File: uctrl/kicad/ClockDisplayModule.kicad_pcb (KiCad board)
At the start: 2 copper layers, 94 x 58.4 mm, 49 parts, among them IC1 ATMEGA88PA-A, P101 CONN_02X03, P102 CONN_01X06, P201 CONN_01X06, P202 CONN_01X07, P203 CONN_01X06, P204 CONN_01X07, Q201 BC856BS, Q202 BC856BS, Q203 BC856BS, SW101 TL3315NF160Q, U201 SN74LS138, U202 74HC4511

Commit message: Updated the revision number
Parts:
- moved P203 2.54 mm to (119.4, 81.3)
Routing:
- net C_Signal: track 7.02 -> 7.72 mm
- net C_Dig_1: track 7.20 -> 7.79 mm
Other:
- board text added: "Clock display Module 2L.5 Control board"
- board text added: "Clock display Module 2L.5 Display board"
- board text removed: "Clock display Module 2L.4 Control board"
- board text removed: "Clock display Module 2L.4 Display board"
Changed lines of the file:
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@@
-(kicad_pcb (version 4) (host pcbnew 4.0.0-stable)
+(kicad_pcb (version 4) (host pcbnew 4.0.0-2.201512072331+6194~38~ubuntu14.04.1-stable)
   (general
     (links 171)
@@
     (thickness 1.6)
     (drawings 25)
-    (tracks 571)
+    (tracks 566)
     (zones 0)
     (modules 49)
@@
   (title_block
     (title "Clock Display Module")
-    (rev 4L.2)
+    (date 2016-05-05)
+    (rev 2L.5)
   )
   (layers
@@
   )
   (setup
-    (last_trace_width 0.1524)
+    (last_trace_width 0.3048)
     (user_trace_width 0.3048)
     (user_trace_width 0.6096)
@@
   )
   (module Pin_Headers:Pin_Header_Straight_1x06 (layer B.Cu)
-    (at 119.38 83.82 180)
+    (at 119.38 81.28 180)
     (descr "Through hole pin header")
     (tags "pin header")
@@
   (gr_line (start 207.01 100.33) (end 115.57 100.33) (angle 90) (layer Edge.Cuts) (width 2.54))
   (gr_line (start 115.57 41.91) (end 207.01 41.91) (angle 90) (layer Edge.Cuts) (width 2.54))
-  (gr_text "Clock display Module 2L.4\nControl board" (at 118.237 80.518) (layer F.SilkS)
+  (gr_text "Clock display Module 2L.5\nControl board" (at 121.666 80.518) (layer F.SilkS)
     (effects (font (size 0.762 0.762) (thickness 0.127)) (justify left))
   )
-  (gr_text "Clock display Module 2L.4\nDisplay board" (at 135.89 73.152) (layer B.SilkS)
+  (gr_text "Clock display Module 2L.5\nDisplay board" (at 135.89 73.152) (layer B.SilkS)
     (effects (font (size 0.762 0.762) (thickness 0.127)) (justify left mirror))
   )
@@
   (segment (start 169.672 93.599) (end 169.672 93.726) (width 0.3048) (layer F.Cu) (net 22))
   (segment (start 155.255 91.178) (end 155.442 90.991) (width 0.3048) (layer F.Cu) (net 22) (status 30))
-  (segment (start 119.38 83.82) (end 121.412 83.82) (width 0.3048) (layer F.Cu) (net 23))
-  (segment (start 121.412 83.82) (end 122.809 82.423) (width 0.3048) (layer F.Cu) (net 23))
-  (segment (start 122.809 82.423) (end 127 82.423) (width 0.3048) (layer F.Cu) (net 23))
-  (segment (start 127 82.423) (end 127.65 83.073) (width 0.3048) (layer F.Cu) (net 23))
-  (segment (start 127.65 83.073) (end 127.65 84.1255) (width 0.3048) (layer F.Cu) (net 23))
-  (segment (start 119.38 86.36) (end 121.539 86.36) (width 0.3048) (layer F.Cu) (net 24))
-  (segment (start 121.539 86.36) (end 122.0985 85.8005) (width 0.3048) (layer F.Cu) (net 24))
-  (segment (start 122.0985 85.8005) (end 126.35 85.8005) (width 0.3048) (layer F.Cu) (net 24))
-  (segment (start 119.38 88.9) (end 123.571 88.9) (width 0.3048) (layer F.Cu) (net 25))
-  (segment (start 123.571 88.9) (end 124.587 87.884) (width 0.3048) (layer F.Cu) (net 25))
-  (segment (start 124.587 87.884) (end 127.254 87.884) (width 0.3048) (layer F.Cu) (net 25))
-  (segment (start 127.254 87.884) (end 127.65 88.28) (width 0.3048) (layer F.Cu) (net 25))
-  (segment (start 127.65 88.28) (end 127.65 89.0785) (width 0.3048) (layer F.Cu) (net 25))
-  (segment (start 119.38 91.44) (end 124.079 91.44) (width 0.3048) (layer F.Cu) (net 26))
-  (segment (start 124.079 91.44) (end 124.7655 90.7535) (width 0.3048) (layer F.Cu) (net 26))
-  (segment (start 124.7655 90.7535) (end 126.35 90.7535) (width 0.3048) (layer F.Cu) (net 26))
-  (segment (start 119.38 93.98) (end 123.063 93.98) (width 0.3048) (layer F.Cu) (net 27))
-  (segment (start 123.063 93.98) (end 123.825 93.218) (width 0.3048) (layer F.Cu) (net 27))
-  (segment (start 123.825 93.218) (end 127.127 93.218) (width 0.3048) (layer F.Cu) (net 27))
-  (segment (start 127.127 93.218) (end 127.523 93.614) (width 0.3048) (layer F.Cu) (net 27))
-  (segment (start 127.523 93.614) (end 127.523 94.4125) (width 0.3048) (layer F.Cu) (net 27))
-  (segment (start 119.38 96.52) (end 123.952 96.52) (width 0.3048) (layer F.Cu) (net 28))
-  (segment (start 123.952 96.52) (end 124.3845 96.0875) (width 0.3048) (layer F.Cu) (net 28))
-  (segment (start 124.3845 96.0875) (end 126.223 96.0875) (width 0.3048) (layer F.Cu) (net 28))
+  (segment (start 127.65 84.1255) (end 127.65 83.073) (width 0.3048) (layer F.Cu) (net 23) (status 400000))
+  (segment (start 125.857 81.28) (end 119.38 81.28) (width 0.3048) (layer F.Cu) (net 23) (status 800000))
+  (segment (start 127.65 83.073) (end 125.857 81.28) (width 0.3048) (layer F.Cu) (net 23))
+  (segment (start 126.35 85.8005) (end 124.7895 85.8005) (width 0.3048) (layer F.Cu) (net 24) (status 400000))
+  (segment (start 122.809 83.82) (end 119.38 83.82) (width 0.3048) (layer F.Cu) (net 24) (status 800000))
+  (segment (start 124.7895 85.8005) (end 122.809 83.82) (width 0.3048) (layer F.Cu) (net 24))
+  (segment (start 127.65 89.0785) (end 127.65 88.407) (width 0.3048) (layer F.Cu) (net 25) (status 400000))
+  (segment (start 125.603 86.36) (end 119.38 86.36) (width 0.3048) (layer F.Cu) (net 25) (status 800000))
+  (segment (start 127.65 88.407) (end 125.603 86.36) (width 0.3048) (layer F.Cu) (net 25))
+  (segment (start 126.35 90.7535) (end 124.7895 90.7535) (width 0.3048) (layer F.Cu) (net 26) (status 400000))
+  (segment (start 122.936 88.9) (end 119.38 88.9) (width 0.3048) (layer F.Cu) (net 26) (status 800000))
+  (segment (start 124.7895 90.7535) (end 122.936 88.9) (width 0.3048) (layer F.Cu) (net 26))
+  (segment (start 127.523 94.4125) (end 127.508 94.3975) (width 0.3048) (layer F.Cu) (net 27) (status C00000))
+  (segment (start 127.508 94.3975) (end 127.508 93.726) (width 0.3048) (layer F.Cu) (net 27) (status 400000))
+  (segment (start 127.508 93.726) (end 125.349 91.567) (width 0.3048) (layer F.Cu) (net 27))
+  (segment (start 125.349 91.567) (end 119.507 91.567) (width 0.3048) (layer F.Cu) (net 27) (status 800000))
+  (segment (start 119.507 91.567) (end 119.38 91.44) (width 0.3048) (layer F.Cu) (net 27) (status C00000))
+  (segment (start 126.223 96.0875) (end 124.1155 93.98) (width 0.3048) (layer F.Cu) (net 28) (status 400000))
+  (segment (start 124.1155 93.98) (end 119.38 93.98) (width 0.3048) (layer F.Cu) (net 28) (status 800000))
   (segment (start 132 83.82) (end 129.667 83.82) (width 0.3048) (layer F.Cu) (net 29))
   (segment (start 129.667 83.82) (end 128.524 84.963) (width 0.3048) (layer F.Cu) (net 29))

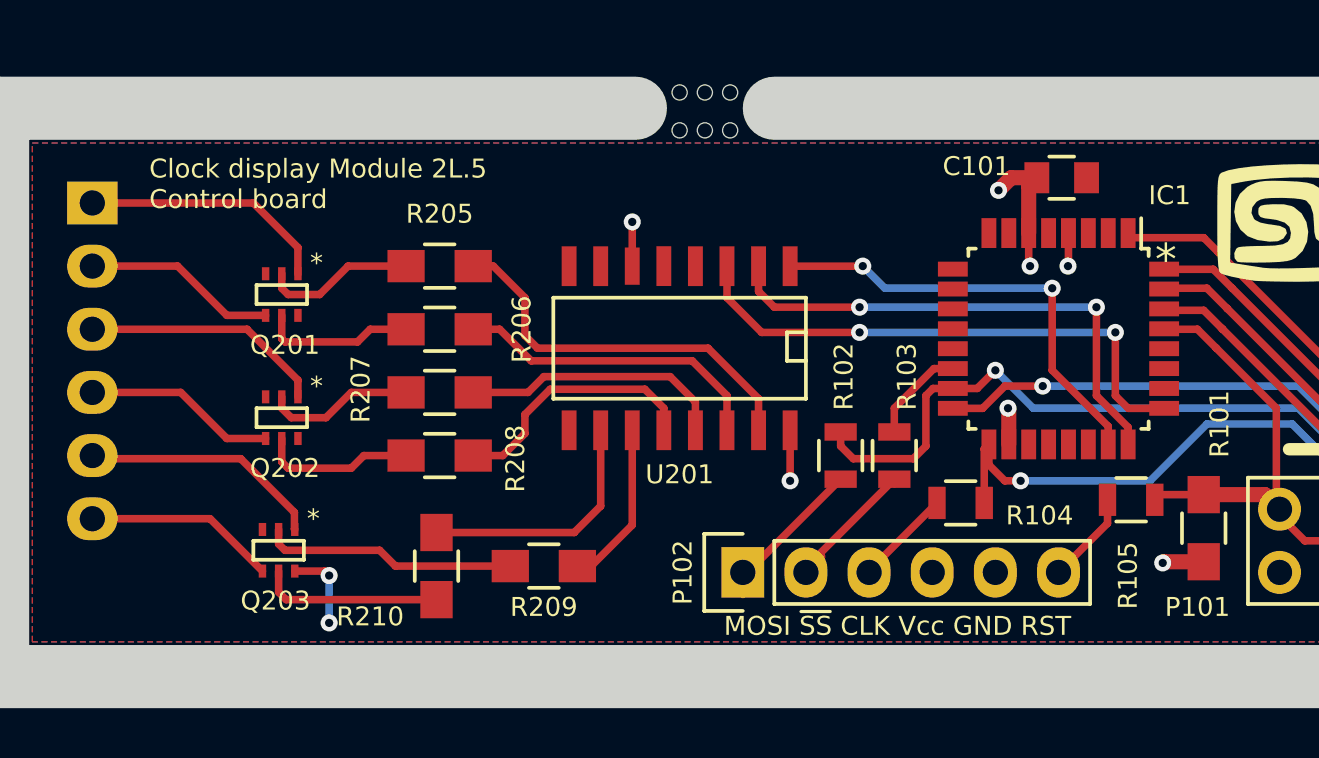
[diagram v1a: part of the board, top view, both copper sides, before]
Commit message: Altered the pin header to include MISO and to simplify connection to to the main board.
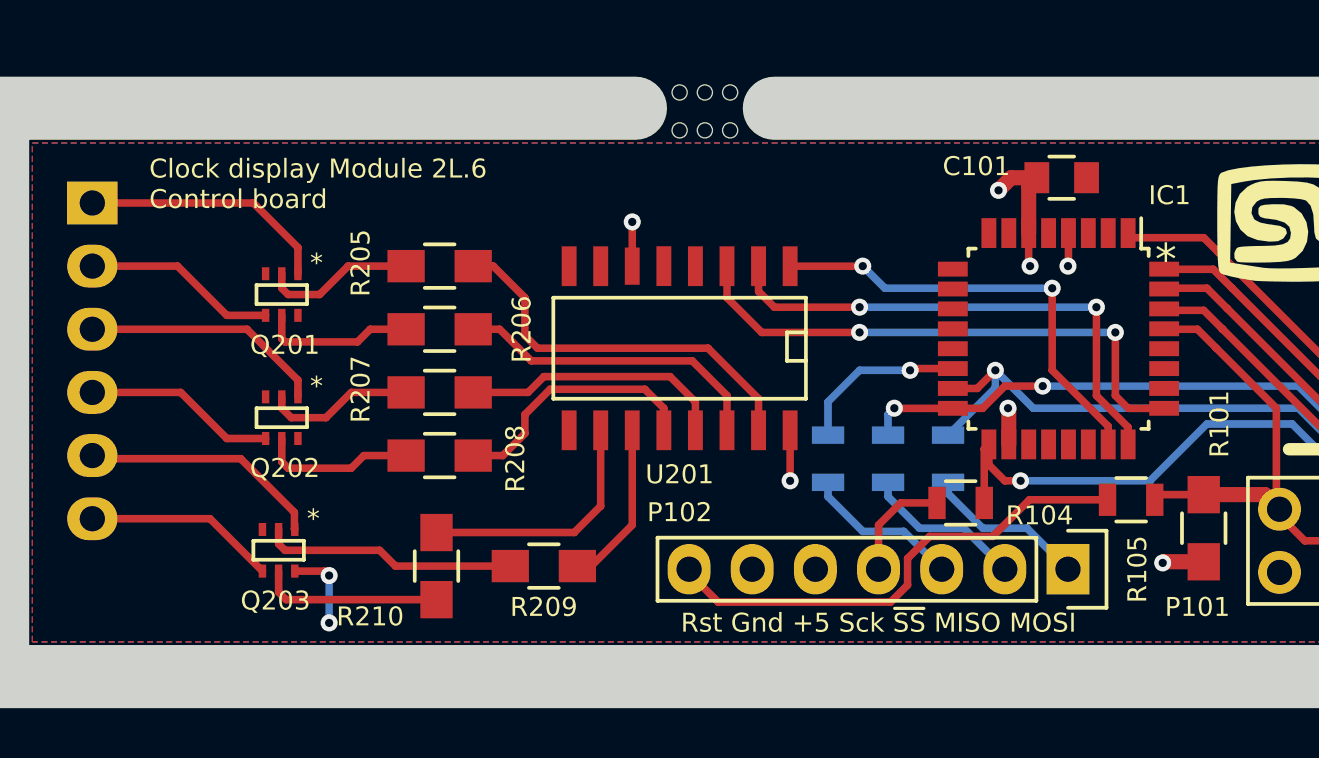
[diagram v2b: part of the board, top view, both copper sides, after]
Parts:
- added R106: 1K, Resistors_SMD:R_0805, B.Cu at (151.4, 91.6)
- P102: value CONN_01X06 -> CONN_01X07; footprint Pin_Headers:Pin_Header_Straight_1x06 -> Pin_Headers:Pin_Header_Straight_1x07
- R102, R103: moved to B.Cu
- moved P102 13.1 mm to (158.6, 96.0), turned to 270 degrees
- moved LOGO1 5.51 mm to (146.2, 72.9)
- moved R102 4.32 mm to (153.8, 91.6)
- moved R103 2.67 mm to (149.0, 91.6)
- renumbered G*** to LOGO1, G*** to LOGO2
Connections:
- IC1 pad 10: (no net) -> Net-(IC1-Pad10)
- IC1 pad 11: (no net) -> Net-(IC1-Pad11)
- IC1 pad 12: (no net) -> Net-(IC1-Pad12)
- IC1 pad 13: (no net) -> Net-(IC1-Pad13)
- IC1 pad 19: (no net) -> Net-(IC1-Pad19)
- IC1 pad 2: (no net) -> Net-(IC1-Pad2)
- IC1 pad 20: (no net) -> Net-(IC1-Pad20)
- IC1 pad 22: (no net) -> Net-(IC1-Pad22)
- IC1 pad 26: (no net) -> Net-(IC1-Pad26)
- IC1 pad 27: (no net) -> Net-(IC1-Pad27)
- IC1 pad 28: (no net) -> Net-(IC1-Pad28)
- IC1 pad 7: (no net) -> Net-(IC1-Pad7)
- IC1 pad 8: (no net) -> Net-(IC1-Pad8)
- IC1 pad 9: (no net) -> Net-(IC1-Pad9)
- P102 pad 4: VCC -> Net-(P102-Pad4)
- P102 pad 5: GND -> VCC
- P102 pad 6: Net-(P102-Pad6) -> GND
- R103 pad 1: Net-(P102-Pad2) -> Net-(P102-Pad3)
- R104 pad 1: Net-(P102-Pad3) -> Net-(P102-Pad4)
- R105 pad 1: Net-(P102-Pad6) -> Net-(P102-Pad7)
- U201 pad 7: (no net) -> Net-(U201-Pad7)
- U201 pad 9: (no net) -> Net-(U201-Pad9)
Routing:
- net Net-(P102-Pad7): track 0.00 -> 19.8 mm
- net Net-(P102-Pad4): track 0.00 -> 4.50 mm
- net MOSI: track 30.9 -> 26.6 mm
- net Net-(P102-Pad6): track 3.74 -> 0.00 mm
- net MISO: track 21.6 -> 25.1 mm, vias 1 -> 2
- net ~SS: track 3.97 -> 6.91 mm, vias 0 -> 1
- net Net-(P102-Pad3): track 3.93 -> 6.36 mm
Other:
- board text added: "4.0.0"
- board text added: "Clock display Module 2L.6 Control board"
- board text added: "Clock display Module 2L.6 Display board"
- board text added: "Rst Gnd +5 Sck ~SS~ MISO MOSI"
- board text removed: "Clock display Module 2L.5 Control board"
- board text removed: "Clock display Module 2L.5 Display board"
- board text removed: "MOSI ~SS~ CLK Vcc GND RST"

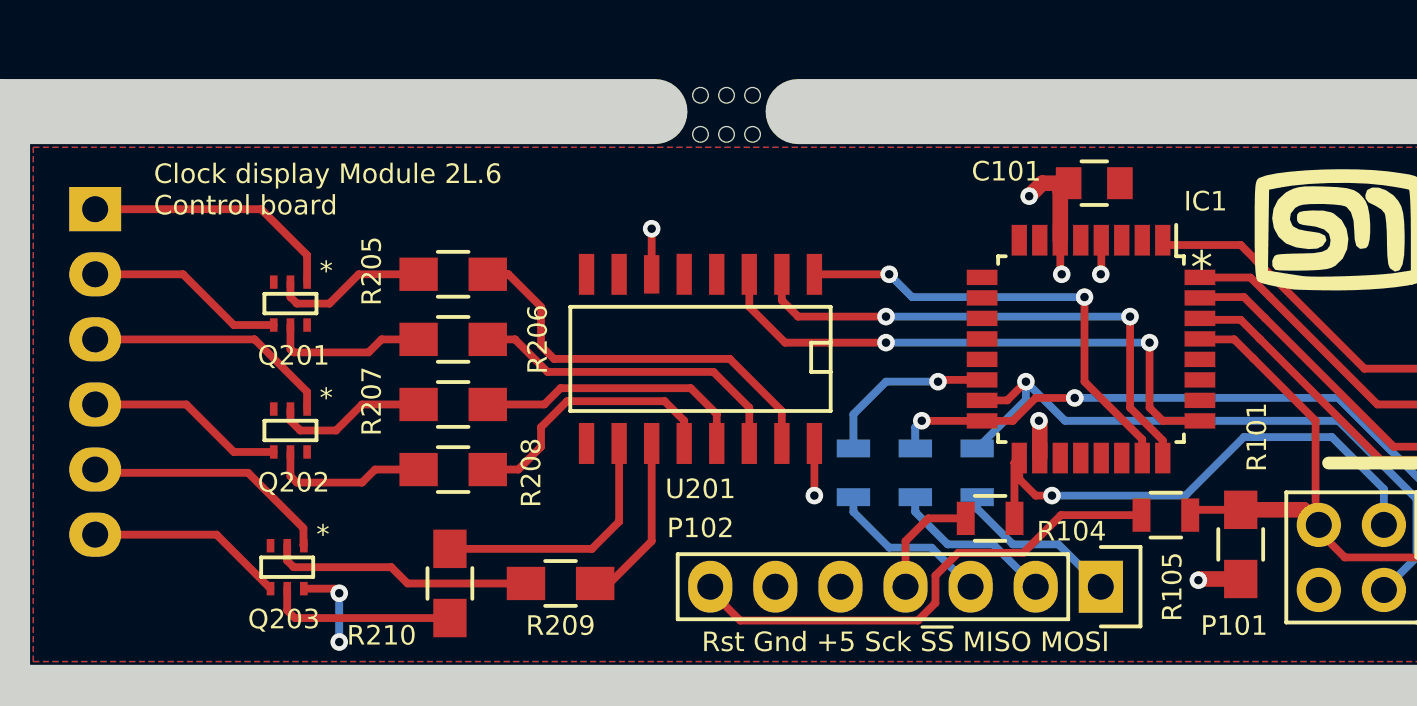
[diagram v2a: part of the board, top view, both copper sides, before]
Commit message: Created 2L_5 Gerbers and ordered stensils and bgoards
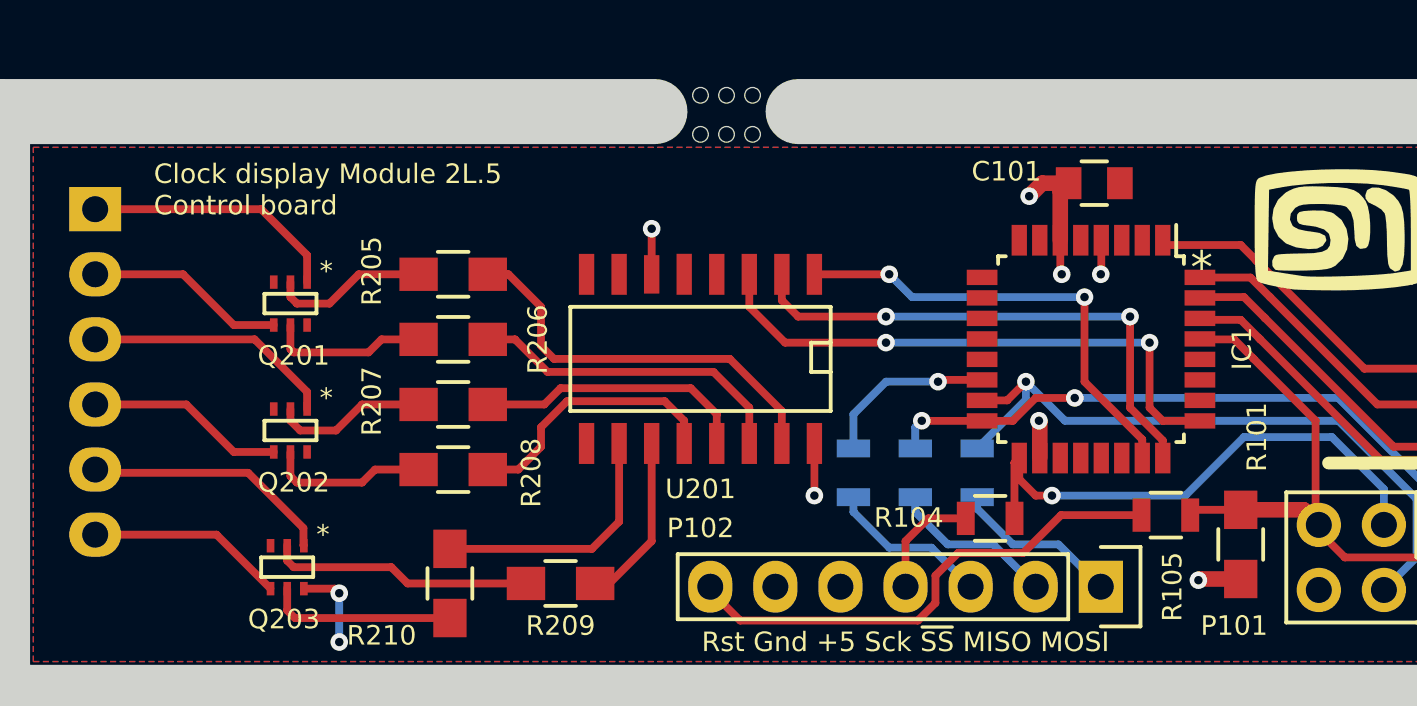
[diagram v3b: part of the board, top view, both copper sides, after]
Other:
- board text added: "Clock display Module 2L.5 Control board"
- board text added: "Clock display Module 2L.5 Display board"
- board text removed: "Clock display Module 2L.6 Control board"
- board text removed: "Clock display Module 2L.6 Display board"
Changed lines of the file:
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@@
   )
   (setup
-    (last_trace_width 0.3048)
+    (last_trace_width 0.1524)
     (user_trace_width 0.3048)
     (user_trace_width 0.6096)
@@
     (tags "QFP 0.8")
     (attr smd)
-    (fp_text reference IC1 (at -5.7658 -4.4704 360) (layer F.SilkS)
+    (fp_text reference IC1 (at -0.0254 -5.8928 450) (layer F.SilkS)
       (effects (font (size 0.762 0.762) (thickness 0.127)))
     )
@@
     (tags "resistor 0805")
     (attr smd)
-    (fp_text reference R104 (at 3.175 0.508) (layer F.SilkS)
+    (fp_text reference R104 (at -3.175 -0.0254) (layer F.SilkS)
       (effects (font (size 0.762 0.762) (thickness 0.127)))
     )
@@
   (gr_line (start 208.28 77.47) (end 181.102 77.47) (angle 90) (layer Edge.Cuts) (width 2.54))
   (gr_line (start 146.812 77.47) (end 175.514 77.47) (angle 90) (layer Edge.Cuts) (width 2.54))
-  (gr_text 1 (at 121.539 83.947) (layer B.SilkS)
+  (gr_text 1 (at 121.5136 81.4324) (layer B.SilkS)
     (effects (font (size 0.762 0.762) (thickness 0.127)) (justify mirror))
   )
@@
   (gr_line (start 207.01 100.33) (end 115.57 100.33) (angle 90) (layer Edge.Cuts) (width 2.54))
   (gr_line (start 115.57 41.91) (end 207.01 41.91) (angle 90) (layer Edge.Cuts) (width 2.54))
-  (gr_text "Clock display Module 2L.6\nControl board" (at 121.666 80.518) (layer F.SilkS)
+  (gr_text "Clock display Module 2L.5\nControl board" (at 121.666 80.518) (layer F.SilkS)
     (effects (font (size 0.762 0.762) (thickness 0.127)) (justify left))
   )
-  (gr_text "Clock display Module 2L.6\nDisplay board" (at 141.859 73.279) (layer B.SilkS)
+  (gr_text "Clock display Module 2L.5\nDisplay board" (at 141.859 73.279) (layer B.SilkS)
     (effects (font (size 1.016 1.016) (thickness 0.1524)) (justify left mirror))
   )
